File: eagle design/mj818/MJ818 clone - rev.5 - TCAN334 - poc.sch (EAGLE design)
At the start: 4 parts, among them J101 Power Supply, J102 LED, J103 CAN

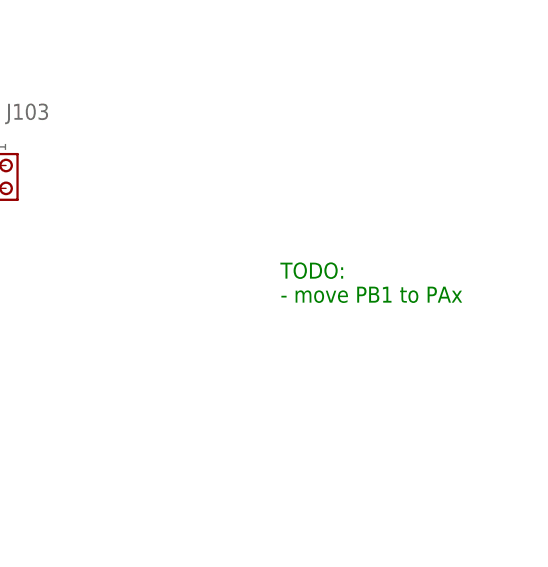
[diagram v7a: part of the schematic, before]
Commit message: mj808/mj818: - moved pins off port B into port A
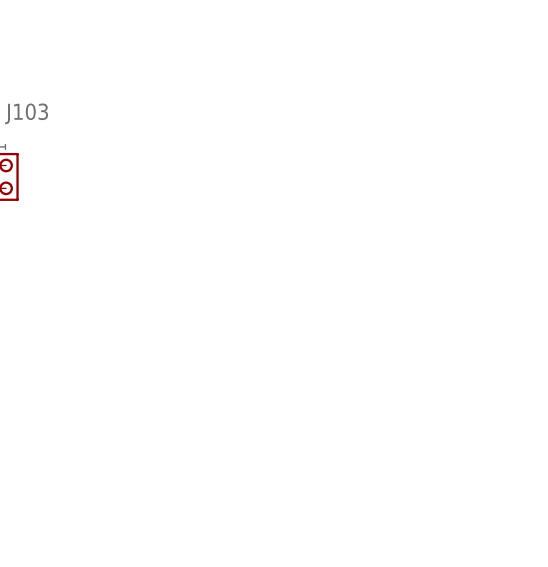
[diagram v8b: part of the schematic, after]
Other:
- note removed: "TODO: - move PB1 to PAx"
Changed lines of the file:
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@@
 <text x="137.16" y="162.56" size="1.778" layer="98">I2C1 SDA</text>
 <text x="137.16" y="152.4" size="1.778" layer="98">external interrupt 0</text>
-<text x="137.16" y="132.08" size="1.778" layer="98">SPI1 MISO</text>
+<text x="167.64" y="132.08" size="1.778" layer="98">SPI1 MISO</text>
 <text x="137.16" y="129.54" size="1.778" layer="98">SPI1 MOSI</text>
 <text x="137.16" y="142.24" size="1.778" layer="98">GPIO</text>
@@
 <text x="137.16" y="81.28" size="1.778" layer="98">USART1 rx</text>
 <text x="137.16" y="86.36" size="1.778" layer="98">timer3 channel 2</text>
-<text x="167.64" y="119.38" size="1.778" layer="98" align="center-left">timer3 channel4</text>
+<text x="137.16" y="119.38" size="1.778" layer="98" align="center-left">timer3 channel4</text>
 <text x="160.02" y="134.62" size="1.778" layer="98">GPIO</text>
 <text x="137.16" y="88.9" size="1.778" layer="98">GPIO</text>
@@
 <net name="DIM_BRAKE" class="0">
 <segment>
-<label x="149.86" y="119.38" size="1.778" layer="95" xref="yes"/>
-<wire x1="129.54" y1="119.38" x2="149.86" y2="119.38" width="0.1524" layer="91"/>
-<pinref part="IC2" gate="G$1" pin="ADC_IN9,TSC_G3_IO3,TIM1_CH3N,TIM3_CH4,TIM14_CH1-PB1_15"/>
+<wire x1="129.54" y1="132.08" x2="149.86" y2="132.08" width="0.1524" layer="91"/>
+<pinref part="IC2" gate="G$1" pin="ADC_IN6,EVENTOUT,TSC_G2_IO3,TIM16_CH1,TIM3_CH1,TIM1_BKIN,SPI1_MISO,I2S1_MCK-PA6_12"/>
+<label x="149.86" y="132.08" size="1.778" layer="95" xref="yes"/>
 </segment>
 </net>
@@
 <wire x1="255.27" y1="191.77" x2="255.27" y2="193.04" width="0.1524" layer="98"/>
 <wire x1="253.365" y1="189.23" x2="257.175" y2="189.23" width="0.1524" layer="98"/>
-<text x="284.48" y="76.2" size="1.778" layer="91">TODO:
-- move PB1 to PAx</text>
 </plain>
 <moduleinsts>
